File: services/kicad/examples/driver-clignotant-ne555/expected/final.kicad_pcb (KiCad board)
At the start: 2 copper layers, 45 x 30 mm, 9 parts, among them J1 PWR_5V, U1 NE555

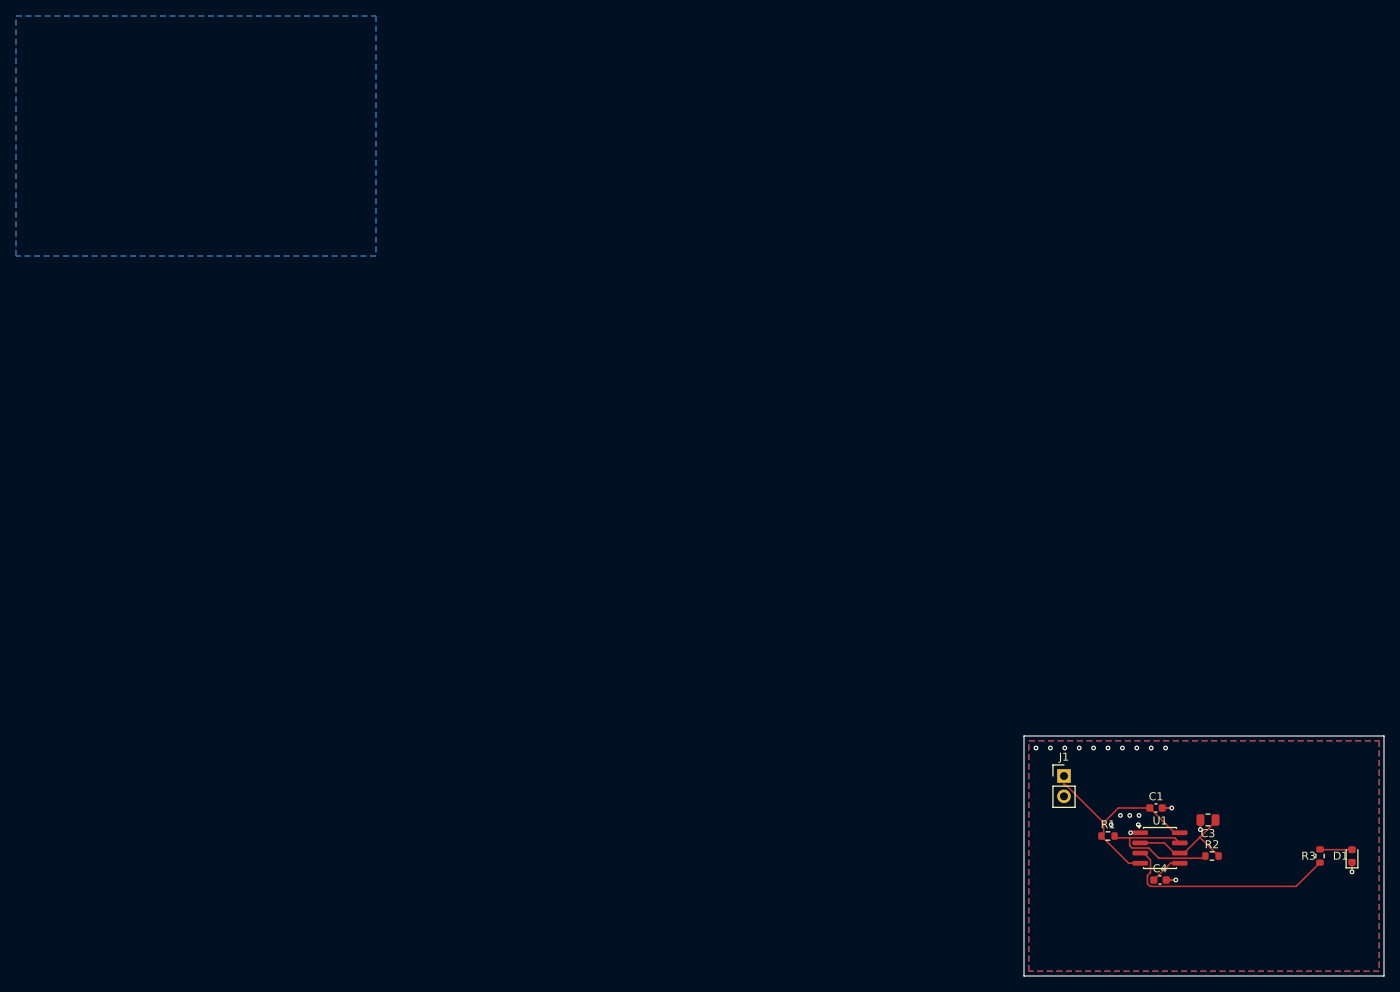
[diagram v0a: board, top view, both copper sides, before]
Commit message: banc(rejeu): douze cartes hors le banc des dix, et le trou qu elles ont revele
Demande : refaire placement et routage de toutes les cartes d `examples/`
SAUF les dix du banc, sans toucher `stm32-validation` ni `STM32-Test`.

DOUZE CARTES REJOUEES, DEUX FAMILLES.

  groupe A (input/schema.json)        regenerer_le_banc.py — garde le meilleur
      carte-11-croisements            100 % · 0 err · 0 perdu   GARDE
      driver-clignotant-ne555         100 % · 0 err · 0 perdu   GARDE
      driver-stm32-minimal            100 % · 0 err · 0 perdu   GARDE
      driver-thermometre-i2c          100 % · 0 err · 0 perdu   GARDE

  groupe B (input/circuit.json)       banc_exemples.py — ecrit dans output/
      arduino-uno       2 couches  100 %  0 manq  0 err    925 s
      esp32-baseline    2 couches  100 %  0 manq  0 err    387 s
      led-blinker       2 couches  100 %  0 manq  0 err    124 s
      nucleo-f401       4 couches   98 %  1 manq  0 err   1814 s
      stm32-baseline    2 couches  100 %  0 manq  0 err    193 s
      stm32-30          2 couches  100 %  0 manq  0 err    404 s
      stm32-60          2 couches  100 %  0 manq  0 err    414 s
      stm32-100         2 couches  100 %  0 manq  0 err    308 s

LE REJEU CONFIRME LES BOARDS LIVRES — ON NE REMPLACE RIEN.

DRC des boards VERSIONNES face aux boards du rejeu, meme instrument
(`kicad-cli pcb drc --severity-all`) des deux cotes :

      sept cartes            0 err · 0 manq des DEUX cotes   egalite
      nucleo-f401            0 manq versionne, 1 au rejeu    on garde l ancien

Livrer des boards de qualite identique ferait du bruit sans rien apporter, et
le tirage de `nucleo-f401` est moins bon : la protection a joue exactement
comme prevu.

LE TROU : CES HUIT CARTES N AVAIENT AUCUN `mesures.json`.

Leur board etait livre depuis le 2026-09-07 et RIEN ne disait ce qu il valait.
Un lecteur ne pouvait ni le verifier ni s en apercevoir — c est la faute que ce
depot poursuit partout, appliquee non pas a un compteur mais a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
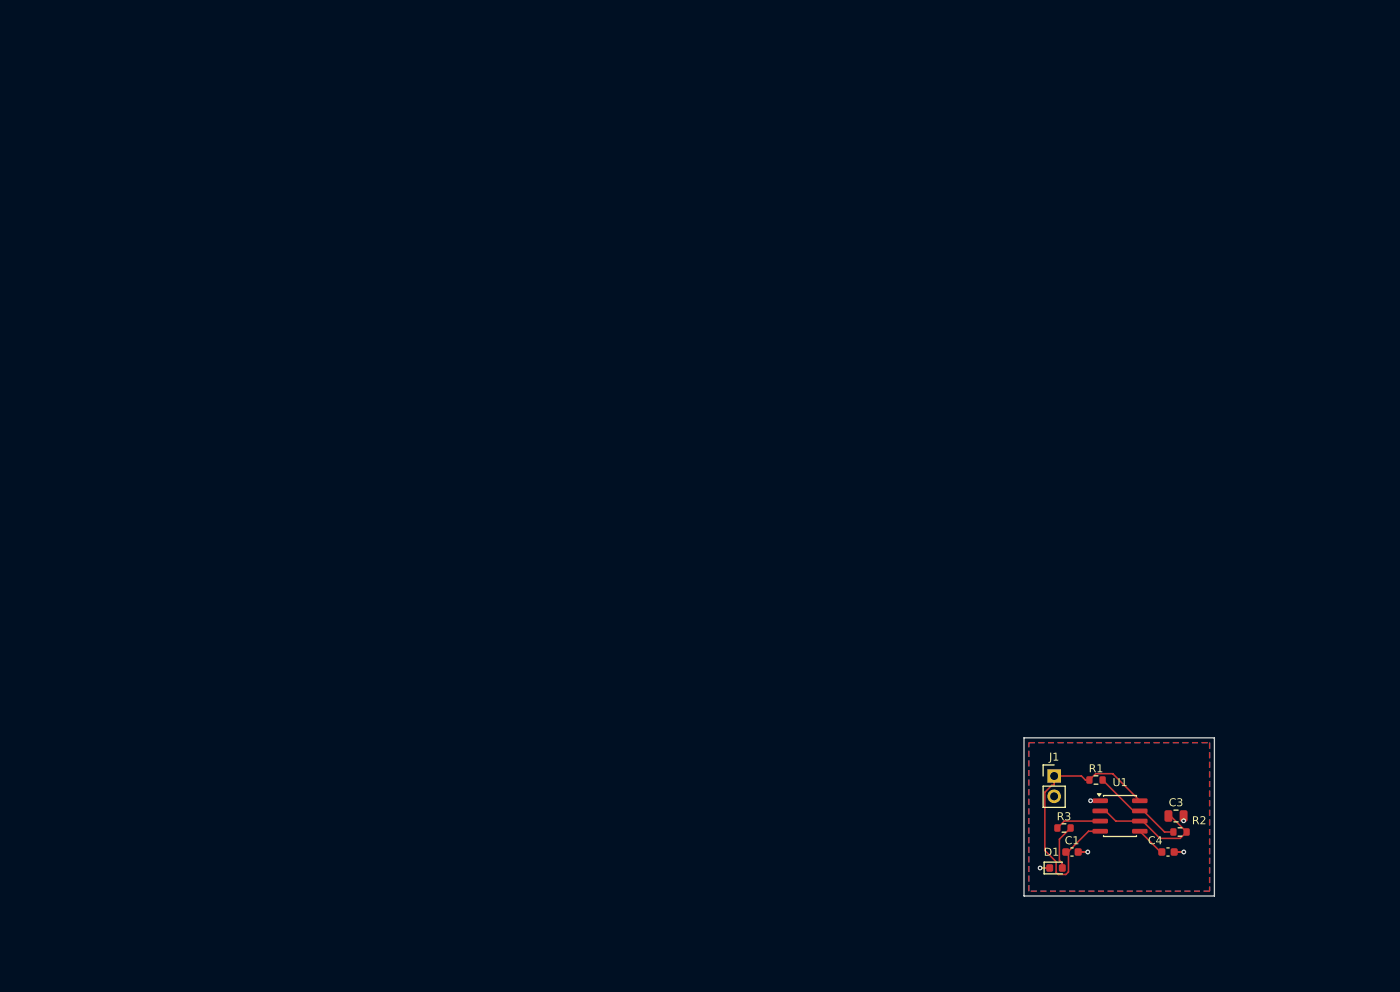
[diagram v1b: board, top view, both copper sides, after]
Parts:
- moved D1 37.0 mm to (130.0, 106.5), turned to 0 degrees
- moved R3 32.2 mm to (131.0, 101.5), turned to 0 degrees
- moved C1 11.9 mm to (132.0, 104.5)
- moved R1 7.16 mm to (135.0, 95.5)
- moved U1 6.40 mm to (138.0, 100.0)
- moved R2 5.00 mm to (145.5, 102.0)
- moved C3 4.03 mm to (145.0, 100.0), turned to 0 degrees
- moved C4 3.64 mm to (144.0, 104.5)
- moved J1 1.23 mm to (129.8, 95.0)
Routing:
- net OUT: track 27.7 -> 5.71 mm
- net DISCH: track 19.7 -> 11.5 mm
- net VCC: track 27.7 -> 35.6 mm
- net LED_A: track 4.02 -> 5.73 mm
- net GND: track 6.00 -> 5.40 mm, vias 20 -> 5
- net THRES: track 15.1 -> 15.7 mm
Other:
- board size 45 x 30 mm -> 23.8 x 19.8 mm
